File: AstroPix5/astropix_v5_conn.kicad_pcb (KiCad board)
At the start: 4 copper layers, 56.4 x 65.6 mm, 50 parts, among them J1 HBOut, J10 SPI_right, J12 Measures_Analog, J14 Bias, J2 Conn_01x05, J3 pcie_GECCO, J4 HBOut, J5 HBOut, J7 HV_in_external, J8 Conn_01x03, J9 SPI_left, U2 AstroPix5_split_powerring

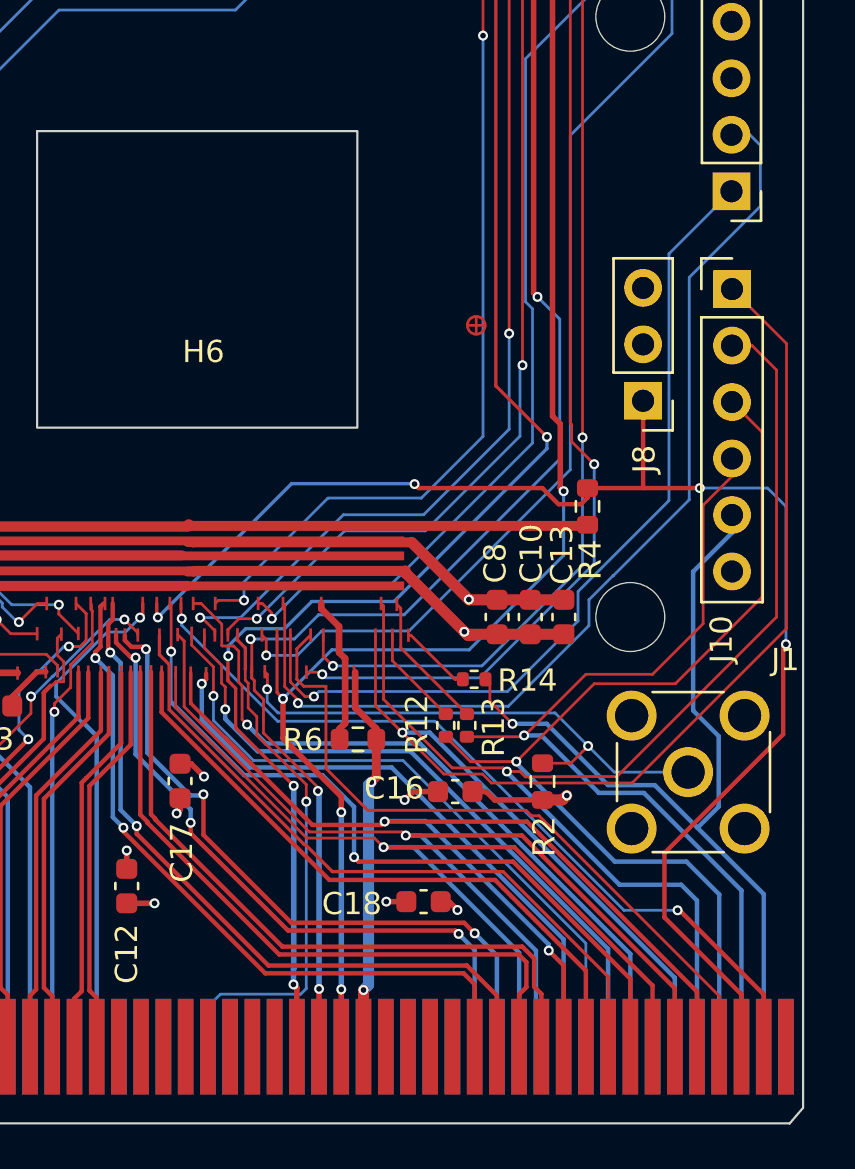
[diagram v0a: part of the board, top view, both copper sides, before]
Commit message: Fix ERC: remove duplicate SR_ck1/SR_ck2/SR_sin labels, fix duplicate PWR_FLAG, regenerate gerbers/PDF/pick-and-place
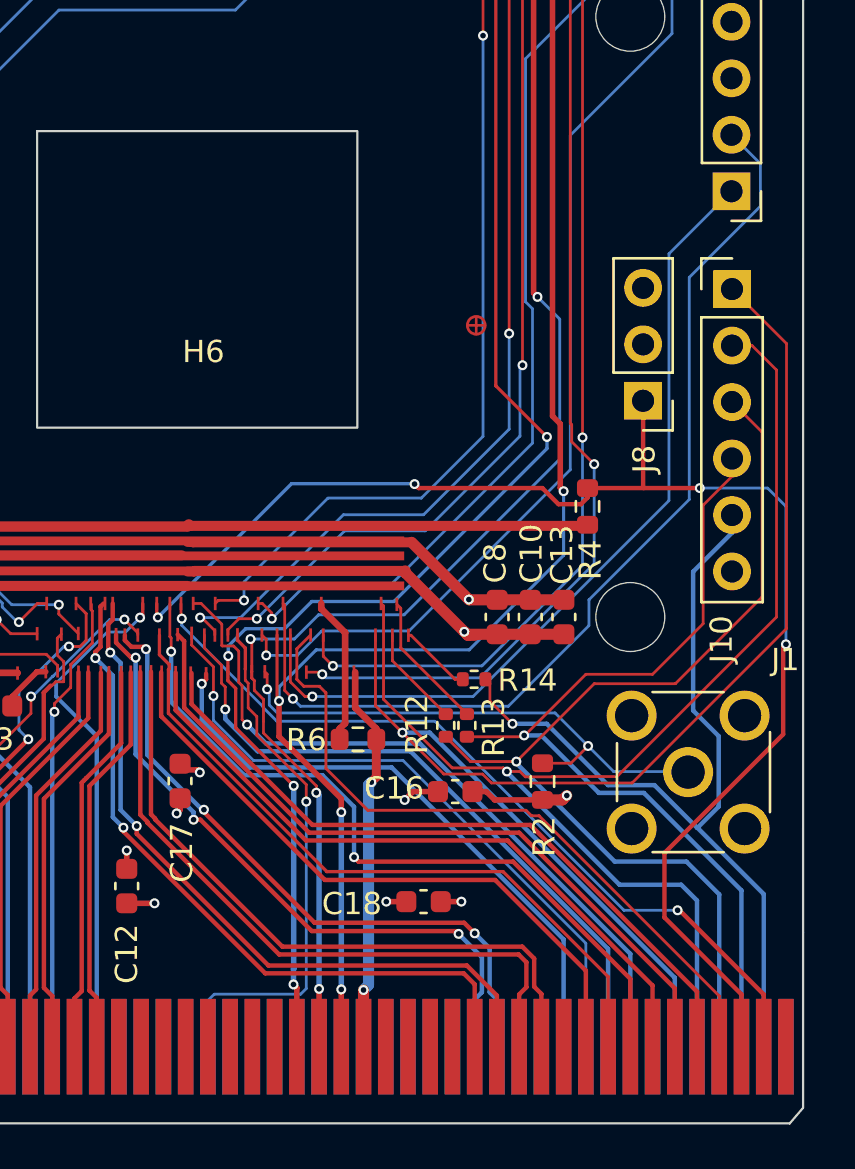
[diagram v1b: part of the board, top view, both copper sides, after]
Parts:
- R6: value 10k -> 0k
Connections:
- J3 pad A42: /SR_ck1 -> unconnected-(J3-FMC_LA13_P-PadA42)
- J3 pad A43: /SR_ck2 -> unconnected-(J3-FMC_LA13_N-PadA43)
- J3 pad B44: /SR_sin -> unconnected-(J3-FMC_LA12_P-PadB44)
- J3 pad B54: /SR_load -> unconnected-(J3-FMC_LA02_P-PadB54)
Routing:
- net /SR_sin: track 46.7 -> 32.0 mm, vias 2 -> 0
- net /SR_ck2: track 45.7 -> 33.3 mm, vias 1 -> 0
- net /SR_ck1: track 43.2 -> 31.0 mm, vias 1 -> 0
- net /SPI_CLK_N: track 30.7 -> 29.8 mm
- net Net-(J12-Pin_1): track 38.9 -> 38.1 mm
- net /VCasc2!: track 89.0 -> 89.6 mm
